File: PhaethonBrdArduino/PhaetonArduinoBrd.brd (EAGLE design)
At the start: 68.6 x 53.3 mm, 25 parts, among them IC1 DS1307, Q1 32.768 Hz, SW1 EC12E_SW

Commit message: Schematic updated
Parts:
- removed U$1: DISCLAIMER, SmartPrj:DISCLAIMER
- added C2: 100nF, rcl:C0805K
- added C_INPUT: 330uF, resistor:140CLH-1010
- added C_OUTPUT: 3.3nF, resistor:140CLH-1010
- added D1: MBRS340T3, diode:SMC
- added IC2: LM2596T, national-semiconductor:T05D
- added L1: 68uH, rcl:L5038P
- added LED1: GM5WA94310A, led:GM5WA94310A
- added R10: 4K, SparkFun:0805
- added R11, R8: 10K\, SparkFun:0805
- added R9: 20K, SparkFun:0805
- added SJ1: (no value), jumper:SJ
- added SL1: (no value), con-amp-quick:04P
- added SV1: (no value), con-amp-mt6:MT6-3
- added T1: (no value), transistor:SOT23-BEC
- added U$2: ADT7301, analogLIB:SOT23-6
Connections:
- net N$1 renamed PIN13
- net N$3 renamed PIN11
- net N$4 renamed PIN12
- net N$6 renamed PIN9
- net N$7 renamed PIN10
- net N$8 renamed PIN0
- removed net N$12: J1.5, J5.5
- removed net N$13: J1.6, J5.6
- removed net N$18: ANALOG.1, J6.1
- removed net N$19: ANALOG.2, J6.2
- removed net N$2: J3.1, J4.1
- removed net N$20: ANALOG.3, J6.3
- new net +24V: C_INPUT.+, IC2.1, R9.1, SV1.3
- new net A0: ANALOG.1, J6.1, LED1.1
- new net A1: ANALOG.2, J6.2, LED1.2
- new net A2: ANALOG.3, J6.3, LED1.3
- new net N$1: D1.C, IC2.2, L1.2
- new net N$10: C_OUTPUT.+, IC2.4, L1.1, SJ1.1
- new net N$11: LED1.4, LED1.5, LED1.6, R11.2
- new net N$9: R10.1, R8.1, T1.B
- new net OUTPUT: R9.2, SV1.1, T1.C
- new net PIN1: J1.2, J5.2
- new net PIN5: J1.6, J5.6, U$2.5
- new net PIN6: J1.7, J5.7, R10.2
- new net SCLK: U$2.4
- net +5V: now also C2.1, SJ1.2, SL1.1, U$2.3
- net GND: now also C2.2, C_INPUT.-, C_OUTPUT.-, D1.A, IC2.3, IC2.5, R11.1, R8.2, SL1.2, SV1.2, T1.E, U$2.1
- net MISO: now also U$2.6
- net MOSI: now also U$2.2
- net PIN2: now also J1.3, J5.3; no longer J1.2, J5.2
- net PIN3: now also J1.4, J5.4; no longer J1.3, J5.3
- net PIN4: now also J1.5, J5.5; no longer J1.4, J5.4
- net PIN7: now also J1.8, J5.8, SL1.3; no longer J1.7, J5.7
- net PIN8: now also J3.1, J4.1, SL1.4; no longer J1.8, J5.8
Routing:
- net N$20: track 2.54 -> 0.00 mm
- net N$19: track 2.54 -> 0.00 mm
- net N$18: track 2.54 -> 0.00 mm
- net A2: track 0.00 -> 2.54 mm
- net A1: track 0.00 -> 2.54 mm
- net A0: track 0.00 -> 2.54 mm
- net PIN6: track 0.00 -> 2.54 mm
- net PIN5: track 0.00 -> 2.54 mm
- net PIN3: track 2.54 -> 0.00 mm
- net PIN2: track 2.54 -> 0.00 mm
- net PIN13: track 2.54 -> 0.00 mm
- net PIN0: track 2.54 -> 0.00 mm
- net N$2: track 2.54 -> 0.00 mm
- net N$13: track 2.54 -> 0.00 mm
- net N$12: track 2.54 -> 0.00 mm

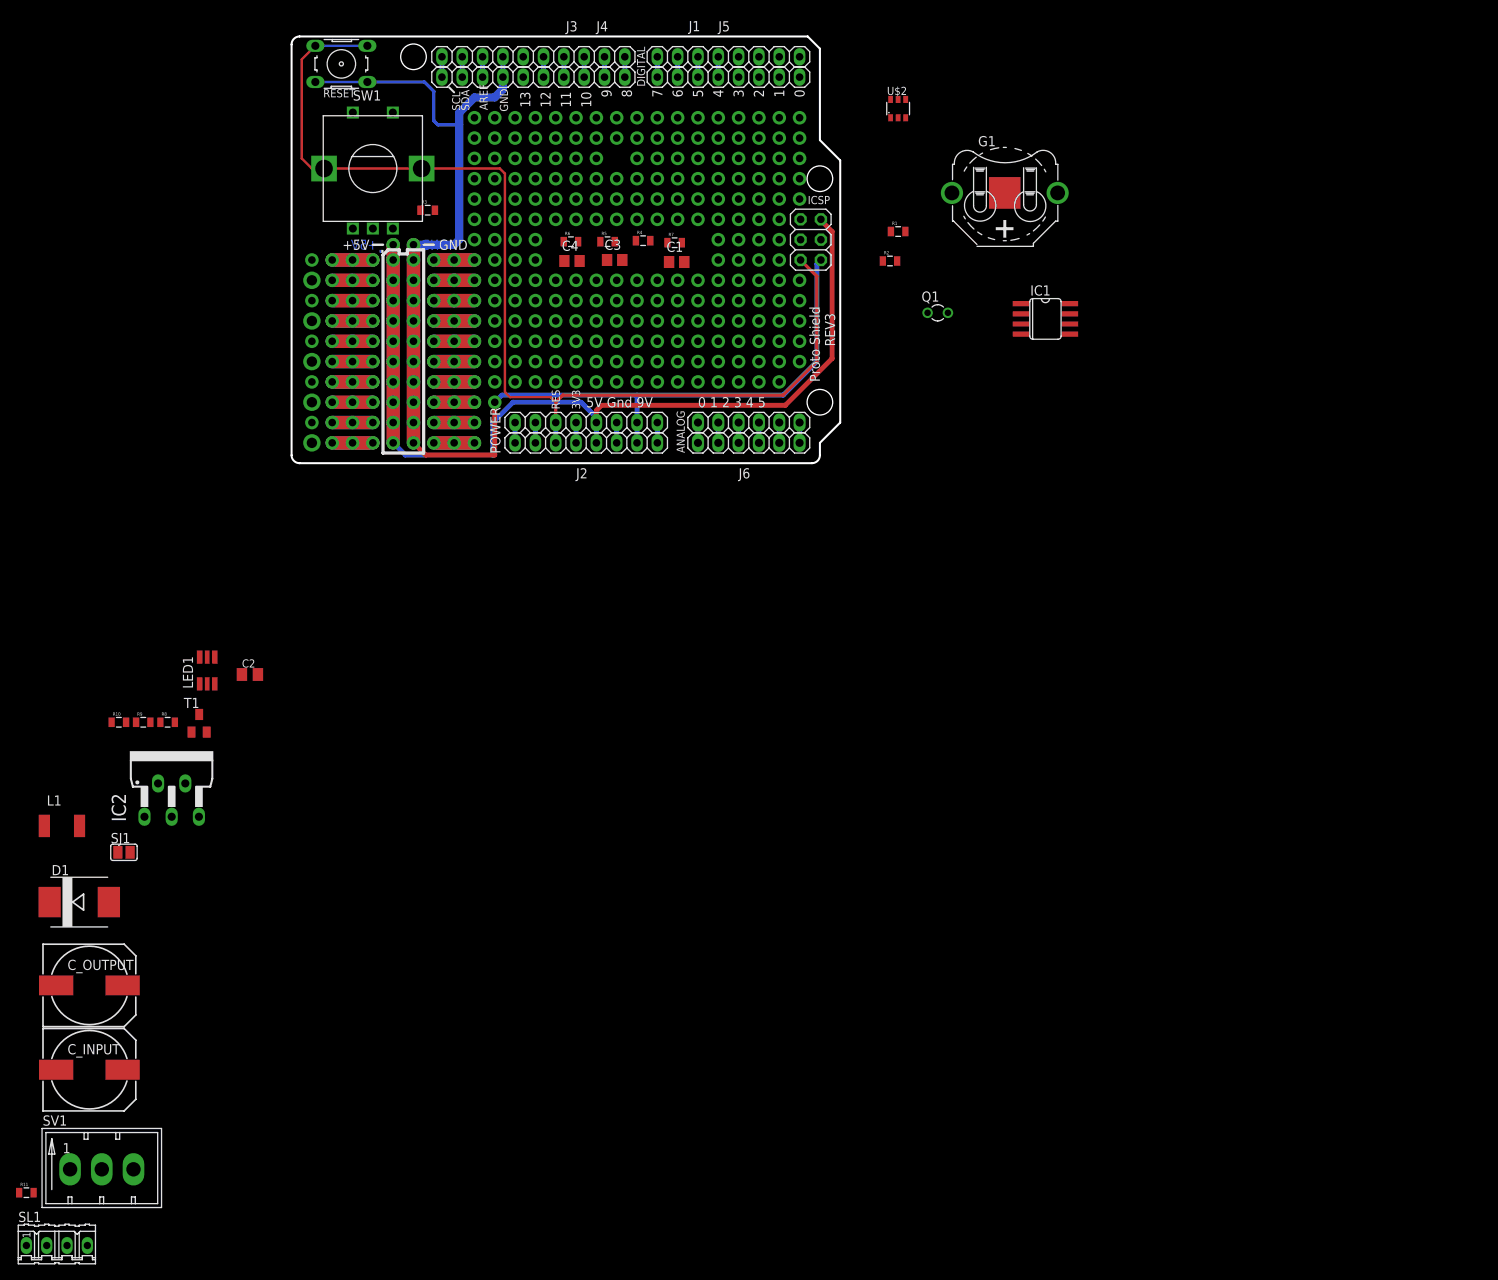
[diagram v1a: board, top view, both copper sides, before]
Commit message: removed from board unusable vias
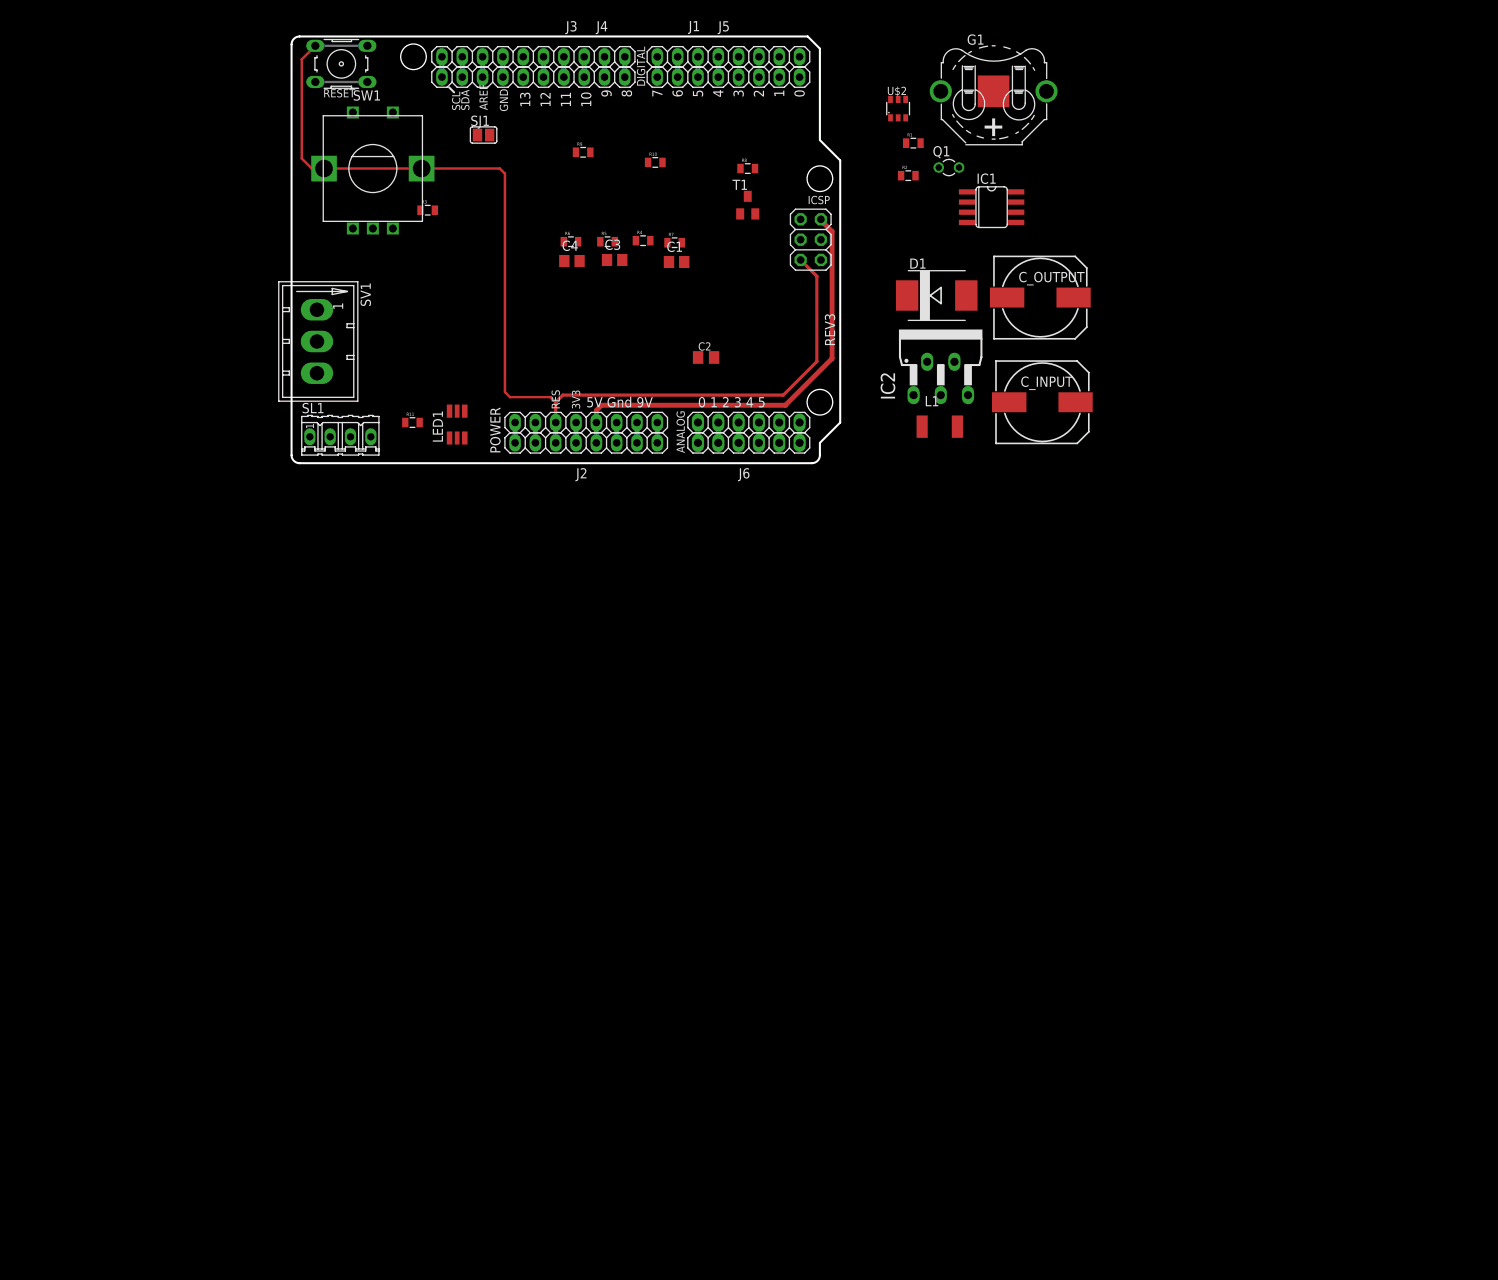
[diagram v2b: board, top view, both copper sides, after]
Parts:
- moved C_OUTPUT 146.7 mm to (93.6, 20.7)
- moved C_INPUT 145.4 mm to (93.9, 7.62)
- moved D1 131.3 mm to (80.6, 21.0)
- moved L1 120.5 mm to (81.0, 4.57)
- moved SV1 114.9 mm to (3.17, 21.7), turned to 270 degrees
- moved IC2 109.6 mm to (81.2, 13.6)
- moved R11 107.7 mm to (15.1, 5.08)
- moved SL1 107.1 mm to (6.10, 3.30)
- moved SJ1 100.3 mm to (24.0, 41.0)
- moved R8 100.2 mm to (57.0, 36.8)
- moved R10 96.9 mm to (45.5, 37.6)
- moved T1 94.3 mm to (57.0, 32.3)
- moved R9 90.0 mm to (36.4, 38.9)
- moved C2 69.4 mm to (51.8, 13.2)
- moved LED1 43.8 mm to (20.7, 4.83)
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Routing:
- net GND: track 183.1 -> 11.6 mm, vias 12 -> 0
- net +5V: track 136.3 -> 54.2 mm, vias 11 -> 0
- net N$87: track 5.08 -> 0.00 mm, vias 2 -> 0
- net N$84: track 5.08 -> 0.00 mm, vias 2 -> 0
- net N$79: track 5.08 -> 0.00 mm, vias 2 -> 0
- net N$67: track 5.08 -> 0.00 mm, vias 2 -> 0
- net N$65: track 5.08 -> 0.00 mm, vias 2 -> 0
- net N$55: track 5.08 -> 0.00 mm, vias 2 -> 0
- net N$41: track 5.08 -> 0.00 mm, vias 2 -> 0
- net N$34: track 5.08 -> 0.00 mm, vias 2 -> 0
- net N$332: track 5.08 -> 0.00 mm, vias 2 -> 0
- net N$178: track 5.08 -> 0.00 mm, vias 2 -> 0
- net N$138: track 5.08 -> 0.00 mm
- net N$137: track 5.08 -> 0.00 mm
- net N$136: track 5.08 -> 0.00 mm
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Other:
- board text removed: "+5V"
- board text removed: "."
- board text removed: "Proto Shield"

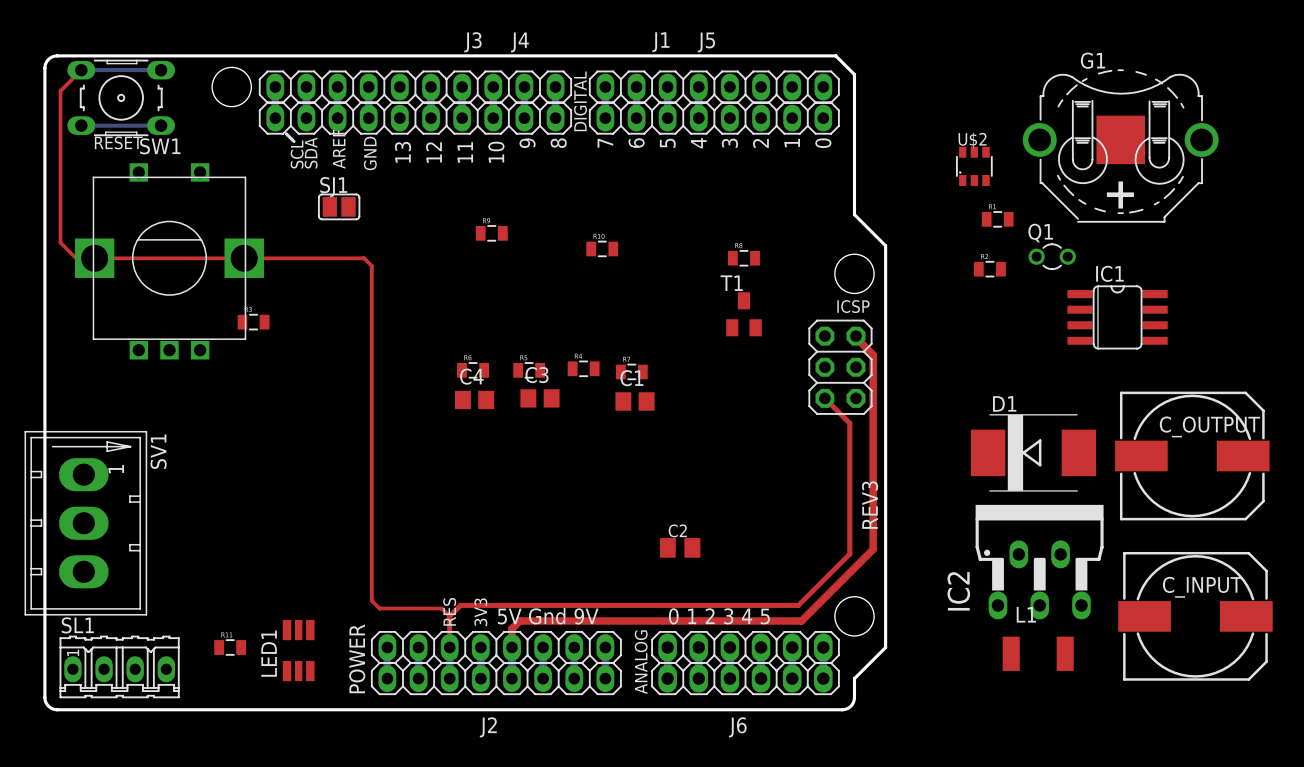
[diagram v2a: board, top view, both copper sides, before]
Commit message: Updated schematic and first board is designed
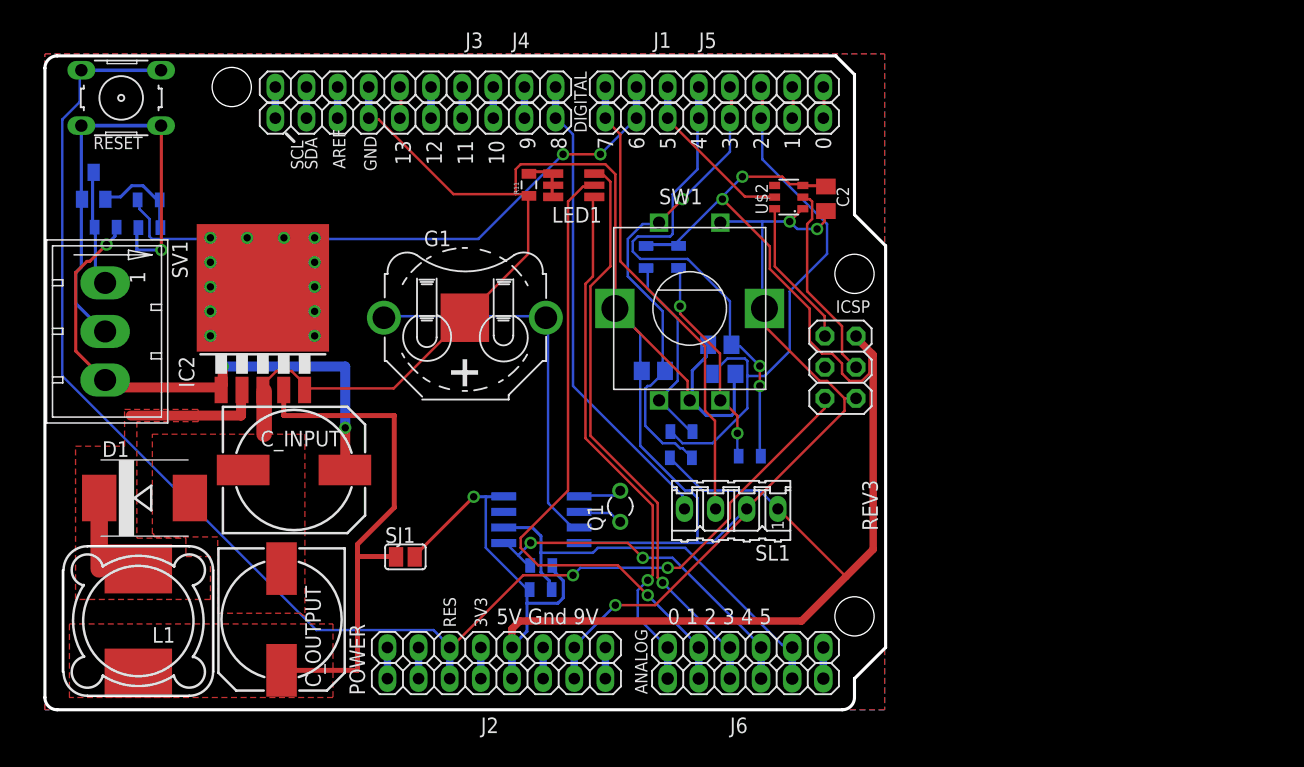
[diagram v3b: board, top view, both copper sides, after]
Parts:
- IC2: value LM2596T -> LM2596S; device national-semiconductor:T05D -> national-semiconductor:TO263-5
- L1: device rcl:L5038P -> inductor-coilcraft:MSS1260
- moved C_OUTPUT 75.5 mm to (19.3, 7.37), turned to 270 degrees
- moved C_INPUT 74.5 mm to (20.3, 19.6)
- moved L1 73.5 mm to (7.62, 7.24), turned to 180 degrees
- moved D1 72.6 mm to (8.13, 17.3)
- moved IC2 66.0 mm to (17.8, 31.9)
- moved G1 55.4 mm to (34.3, 32.0)
- moved T1 54.1 mm to (3.98, 42.7), flipped to the bottom
- moved SL1 51.6 mm to (56.0, 16.4), turned to 180 degrees
- moved IC1 49.8 mm to (40.5, 16.1), flipped to the bottom
- moved R8 48.6 mm to (8.52, 39.3), flipped to the bottom
- moved R1 48.0 mm to (40.4, 9.80), flipped to the bottom
- moved R11 44.9 mm to (39.5, 42.8), turned to 90 degrees
- moved LED1 44.1 mm to (43.1, 42.8), turned to 90 degrees
- moved R2 43.9 mm to (40.5, 11.8), flipped to the bottom, turned to 180 degrees
- moved SW1 42.6 mm to (52.6, 32.7)
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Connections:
- removed net N$1: D1.C, IC2.2, L1.2
- removed net N$10: C_OUTPUT.+, IC2.4, L1.1, SJ1.1
- new net OUTPUT1: D1.C, IC2.2, L1.P$2
- new net OUTPUT5V: C_OUTPUT.+, IC2.4, L1.P$1, SJ1.1
- net GND: now also SW1.GND1, SW1.GND2
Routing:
- net GND: track 11.6 -> 239.4 mm, vias 0 -> 4
- net +5V: track 54.2 -> 144.0 mm, vias 0 -> 3
- net A1: track 2.54 -> 53.0 mm, vias 0 -> 1
- net PIN6: track 2.54 -> 49.8 mm, vias 0 -> 2
- net +24V: track 0.00 -> 45.2 mm, vias 0 -> 3
- net A2: track 2.54 -> 47.6 mm, vias 0 -> 1
- net PIN2: track 0.00 -> 44.6 mm
- net OUTPUT5V: track 0.00 -> 42.5 mm
- net A0: track 2.54 -> 43.4 mm, vias 0 -> 1
- net PIN3: track 0.00 -> 38.9 mm, vias 0 -> 1
- net PIN4: track 2.54 -> 40.9 mm, vias 0 -> 2
- net PIN8: track 2.54 -> 38.8 mm
- net PIN7: track 2.54 -> 38.1 mm
- net SCL: track 2.54 -> 34.7 mm
- net N$97: track 0.00 -> 32.0 mm
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- added copper zone on layer 1, net GND
- added copper zone on layer 16, net GND
- added copper zone on layer 1, net OUTPUT1
- added copper zone on layer 1, net OUTPUT5V

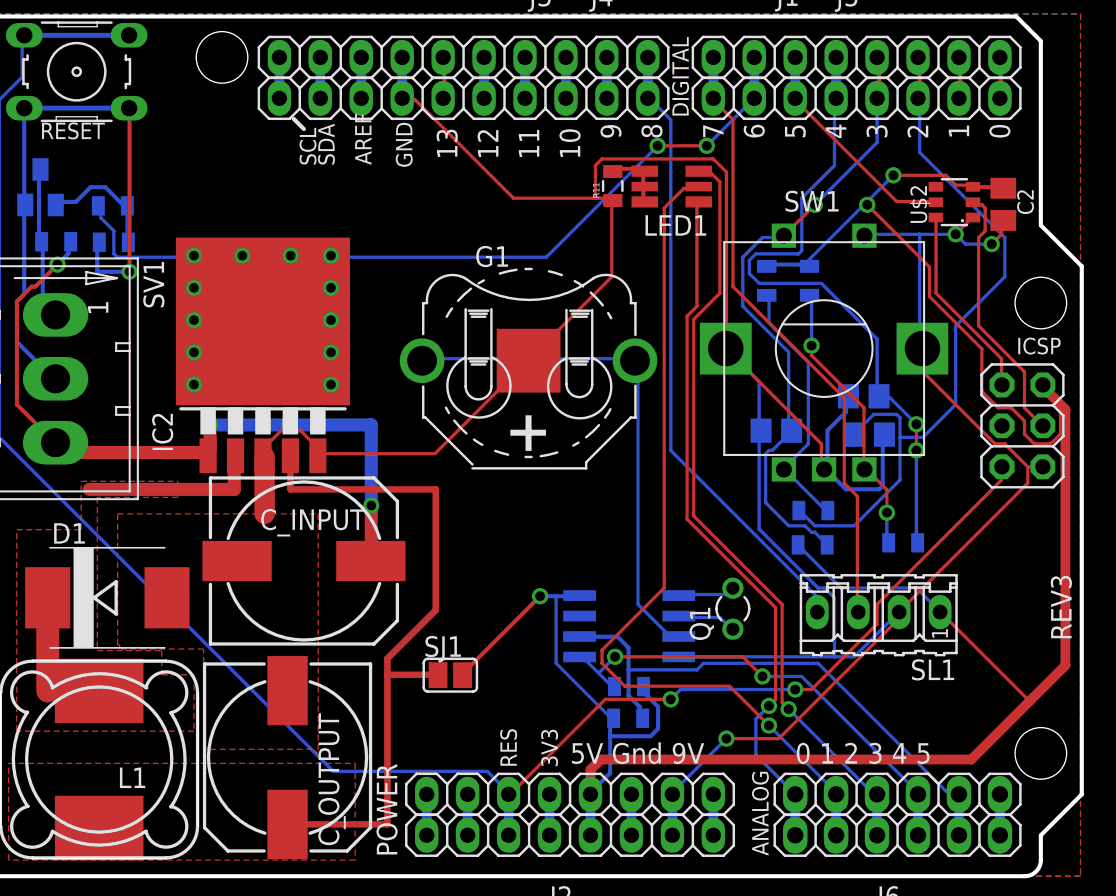
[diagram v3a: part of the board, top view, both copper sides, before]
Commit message: Bug fixed, Temperature sens was not connected
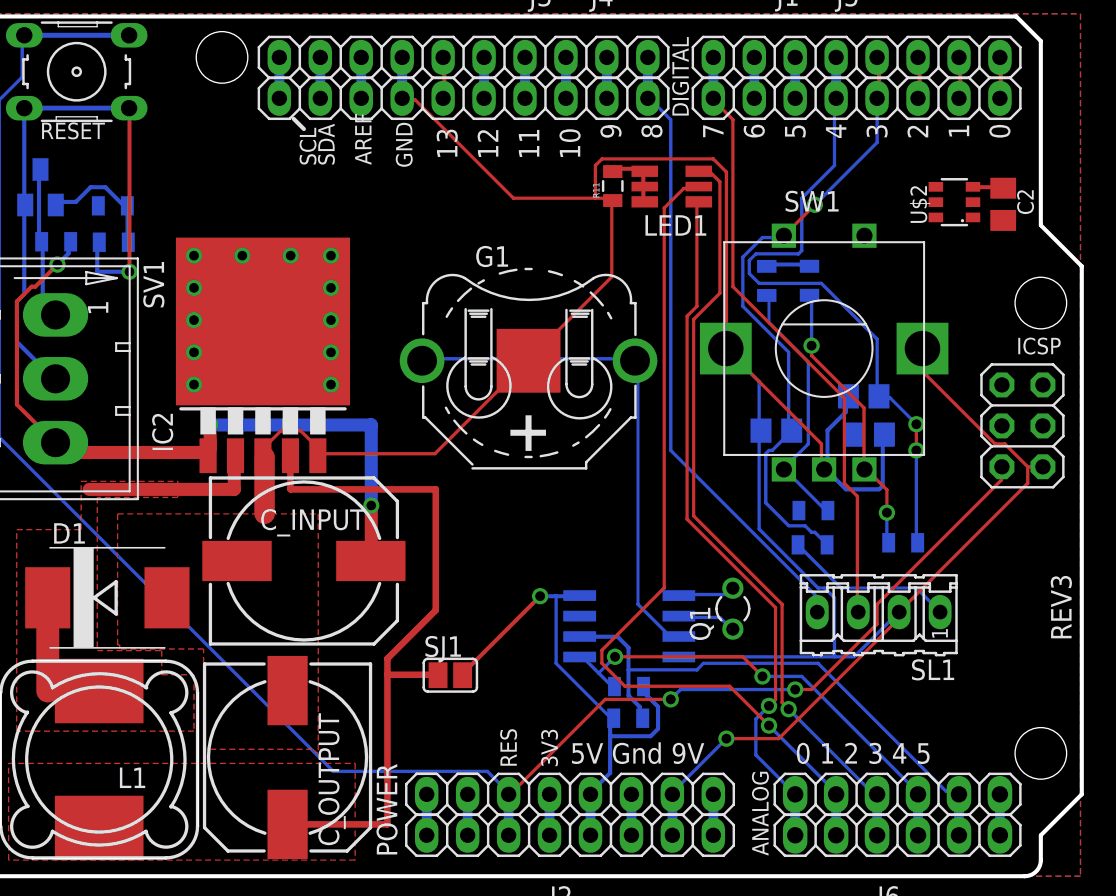
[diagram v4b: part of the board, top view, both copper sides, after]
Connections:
- removed net PIN11: J3.4, J4.4
- removed net PIN12: J3.5, J4.5
- removed net PIN13: J3.6, J4.6
- removed net SCLK: U$2.4
- net MISO: now also J3.5, J4.5
- net MOSI: now also J3.4, J4.4
- net SCK: now also J3.6, J4.6, U$2.4
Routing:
- net +5V: track 144.0 -> 47.8 mm, vias 3 -> 1
- net PIN6: track 49.8 -> 2.54 mm, vias 2 -> 0
- net PIN2: track 44.6 -> 2.63 mm
- net GND: track 239.4 -> 221.2 mm, vias 4 -> 2
- net MOSI: track 16.3 -> 2.54 mm
- net PIN5: track 14.0 -> 2.54 mm
- net MISO: track 12.1 -> 2.54 mm
- net SCK: track 0.00 -> 2.59 mm
- net PIN13: track 2.59 -> 0.00 mm
- net PIN12: track 2.54 -> 0.00 mm
- net PIN11: track 2.54 -> 0.00 mm
